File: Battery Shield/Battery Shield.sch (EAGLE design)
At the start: 3 parts

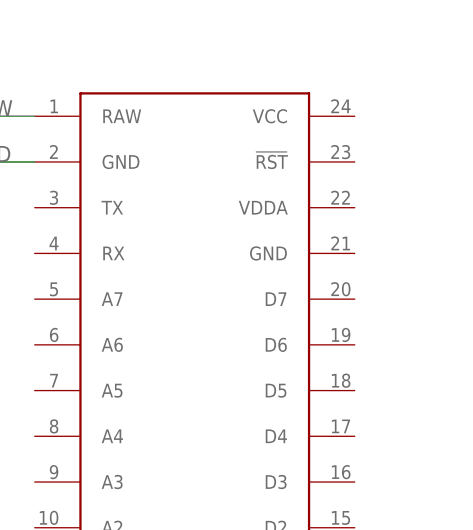
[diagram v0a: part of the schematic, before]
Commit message: Reviewed battery shield and PIR shield. Good to go.
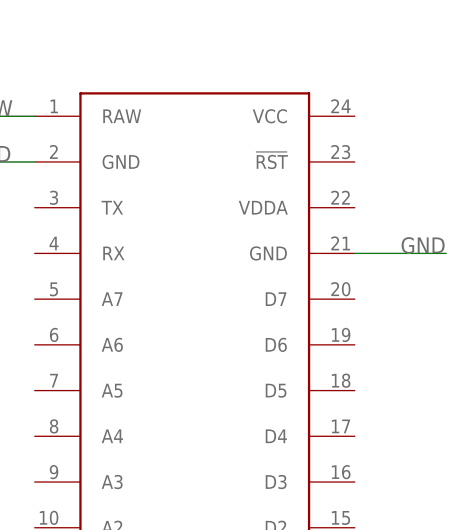
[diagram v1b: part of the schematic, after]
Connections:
- net GND: now also U$1.GND@21
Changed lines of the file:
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@@
 <label x="35.56" y="63.5" size="1.778" layer="95"/>
+</segment>
+<segment>
+<pinref part="U$1" gate="G$1" pin="GND@21"/>
+<wire x1="101.6" y1="60.96" x2="111.76" y2="60.96" width="0.1524" layer="91"/>
+<label x="106.68" y="60.96" size="1.778" layer="95"/>
 </segment>
 </net>
